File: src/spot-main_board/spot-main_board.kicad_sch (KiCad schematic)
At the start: 0 parts

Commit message: Start drawing schematics.
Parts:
- added A1: Arduino_UNO_R3, Module:Arduino_UNO_R3, symbol MCU_Module:Arduino_UNO_R3
- added D1: PTVS7V5Z1USK, Diode_SMD:Nexperia_DSN1608-2_1.6x0.8mm, symbol Diode:PTVS7V5Z1USK
- added EFB1, J1: Conn_01x02, symbol Connector_Generic:Conn_01x02
- added EFB2: Microwave Oven Transformer, symbol Transformer:TEZ0.5-D-1
- added EFB?: RED, symbol Device:LED
- added EFB?: BLUE, symbol Device:LED
- added J3: AudioJack2, symbol Connector_Audio:AudioJack2
- added J?: Screw_Terminal_01x08, symbol Connector:Screw_Terminal_01x08
- added PS2: TMF05112, Converter_ACDC:Converter_ACDC_TRACO_TMF_051xx_THT, symbol Converter_ACDC:TMF05112
- added Q1: BT139-600, Package_TO_SOT_THT:TO-220-3_Vertical, symbol Triac_Thyristor:BT139-600
- added Q2: Q_PMOS_DGS, symbol Transistor_FET:Q_PMOS_DGS
- added R? (x2): 470, symbol Device:R
- added RV1: R_Potentiometer, symbol Device:R_Potentiometer
- added U1: MOC3041M, symbol Relay_SolidState:MOC3041M
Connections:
- new net: J?.4 (Pin_4), R?.2
- new net: J?.5 (Pin_5), R?.2
- new net: A1.11 (A2), J?.7 (Pin_7)
- new net: A1.25 (D10), R?.1
- new net: A1.26 (D11), R?.1
- new net +12V: A1.8 (VIN), J?.6 (Pin_6), Q2.3 (S)
- new net +DC_OUT: D1.1 (K), PS2.4 (+Vout), Q2.1 (D)
- new net AC_L: J1.1 (Pin_1), PS2.1 (AC(L))
- new net AC_N: J1.2 (Pin_2), PS2.2 (AC(N)), Q1.2 (A2)
- new net CONN_+5V: RV1.1
- new net CONN_GND: EFB?.1 (K), EFB?.1 (K), RV1.3
- new net GND: A1.29 (GND), A1.6 (GND), A1.7 (GND), D1.2 (A), J?.8 (Pin_8), PS2.3 (-Vout), Q2.2 (G)
- no-connect marks 0 -> 12
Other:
- note added: "230 VAC in"
- note added: "External interface"
- note added: "~10 mA"
- title: (none) -> Spot

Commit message: Add Electronics Block Diagram. Continue work on schematics.
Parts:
- removed EFB1: Conn_01x02, symbol Connector_Generic:Conn_01x02
- removed EFB2: Microwave Oven Transformer, symbol Transformer:TEZ0.5-D-1
- removed EFB?: RED, symbol Device:LED
- removed EFB?: BLUE, symbol Device:LED
- removed J3: AudioJack2, symbol Connector_Audio:AudioJack2
- removed RV1: R_Potentiometer, symbol Device:R_Potentiometer
- added J?: Conn_01x02, symbol Connector_Generic:Conn_01x02
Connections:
- net AC_L: now also J?.1 (Pin_1)
- net at J?.2 (Pin_2): now also A1.23 (D8)
- net at J?.3 (Pin_3): now also A1.24 (D9)
- net at Q1.1 (A1): now also J?.2 (Pin_2)
- net +5V: now reaches A1.5 (+5V)
- no-connect marks 12 -> 11
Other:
- note added: "To MOT primary coil"
- note removed: "External interface"
- company: (none) -> Anker Bjerkestrand
- moved on the sheet: A1, D1, J1, J?, PS2, Q1, Q2, R?, U1

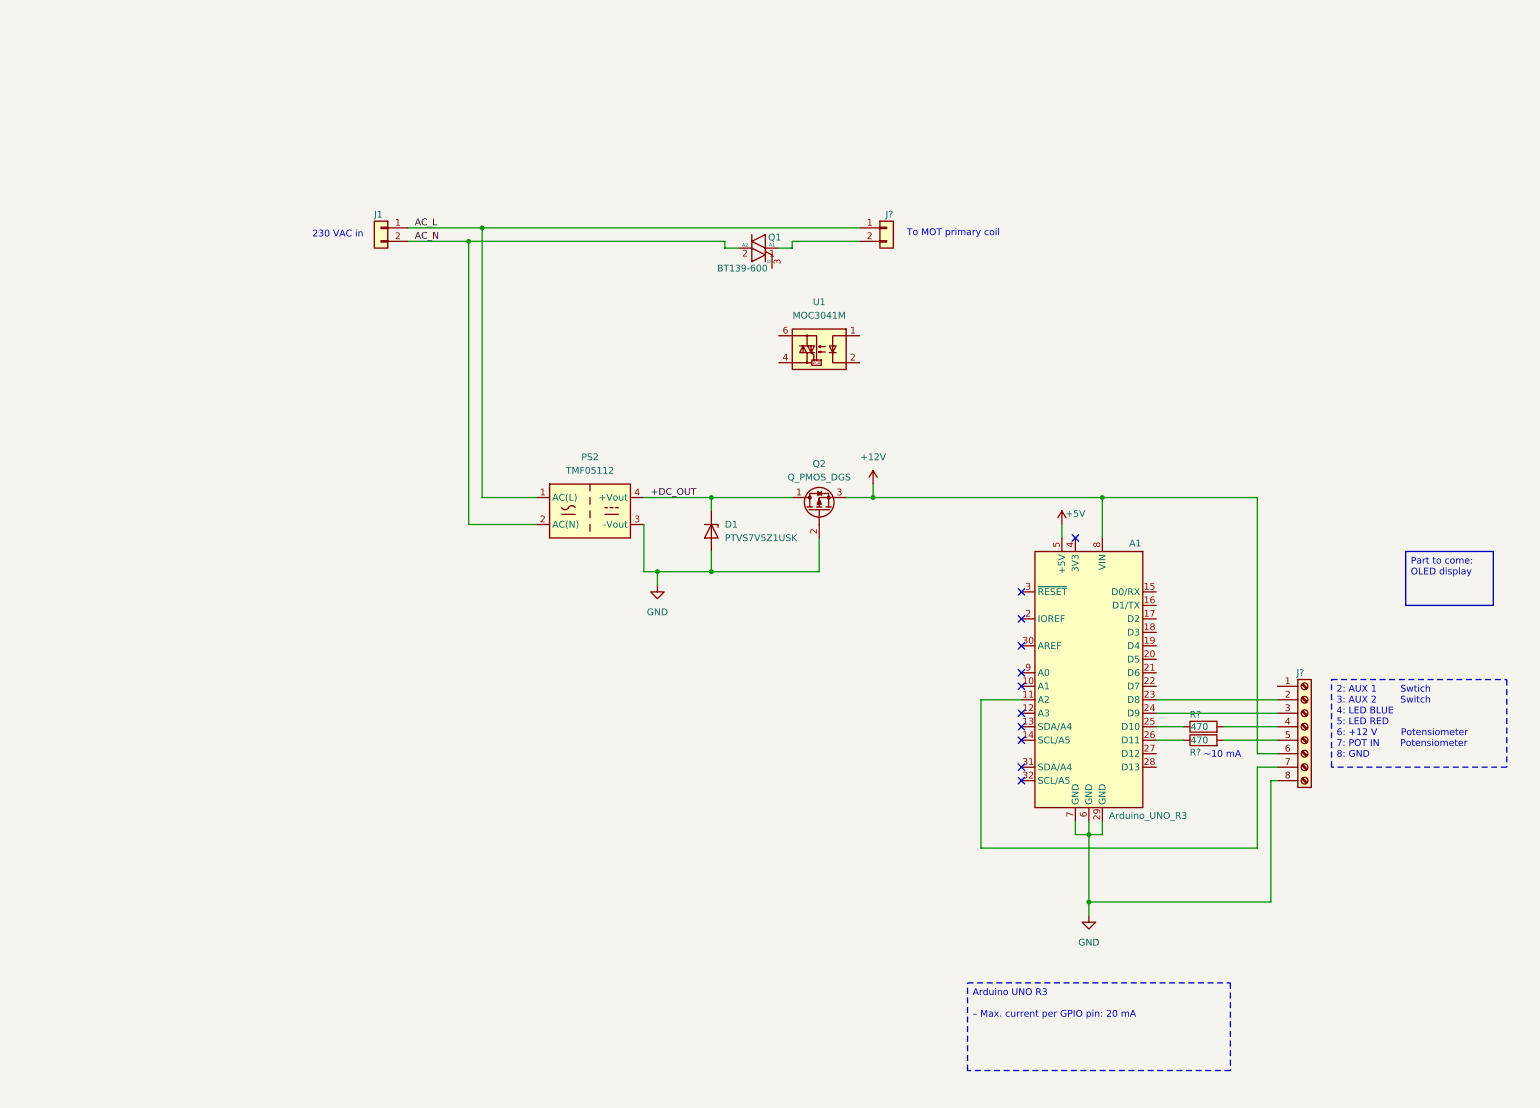
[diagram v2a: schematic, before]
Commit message: Add kidibom.py file. Add example circuitry for triac and driver.
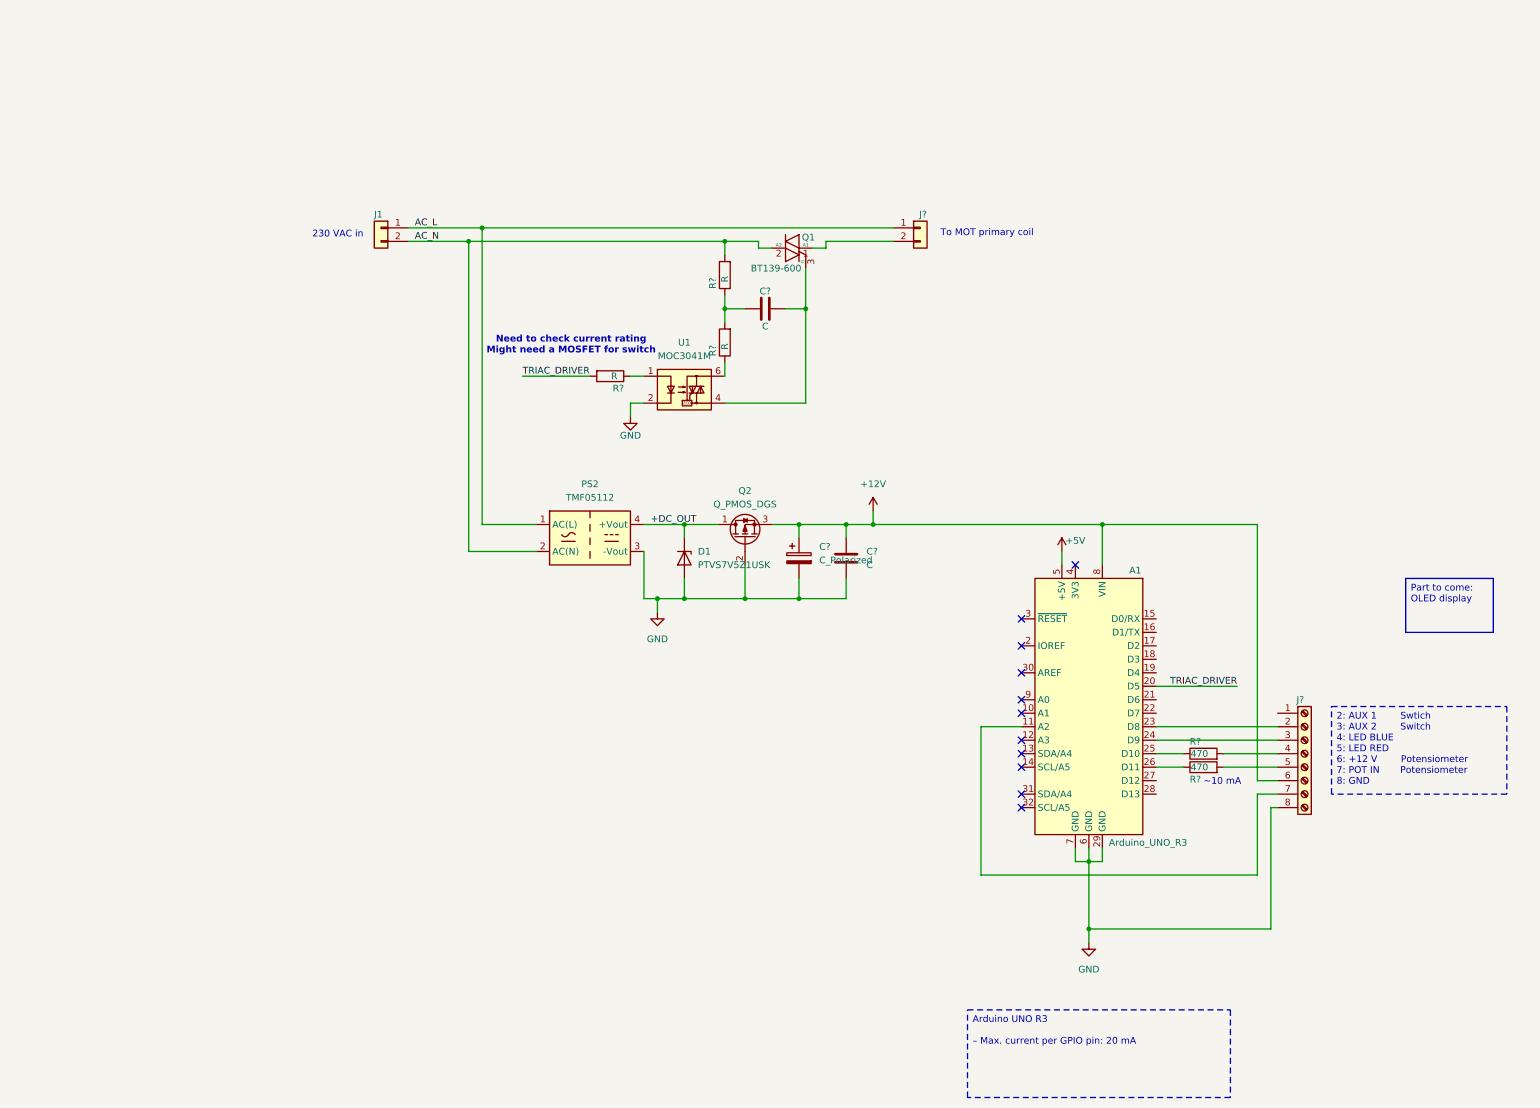
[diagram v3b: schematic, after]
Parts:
- added C?: C_Polarized, symbol Device:C_Polarized
- added C? (x2): C, symbol Device:C
- added R? (x3): R, symbol Device:R
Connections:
- net +12V: now also C?.1, C?.1
- net AC_N: now also R?.2
- net GND: now also U1.2, C?.2, C?.2
- net at Q1.3 (G): now also U1.4, C?.2
- net TRIAC_DRIVER: now reaches A1.20 (D5)
- net TRIAC_DRIVER: now also R?.2
- net at U1.1: now also R?.1
- net at U1.6: now also R?.1
- new net: C?.1, R?.1, R?.2
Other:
- note added: "Need to check current rating Might need a MOSFET for switch"
- moved on the sheet: A1, D1, J?, PS2, Q1, Q2, R?, U1

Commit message: Finish schematics. Start adding footprints and choosing components.
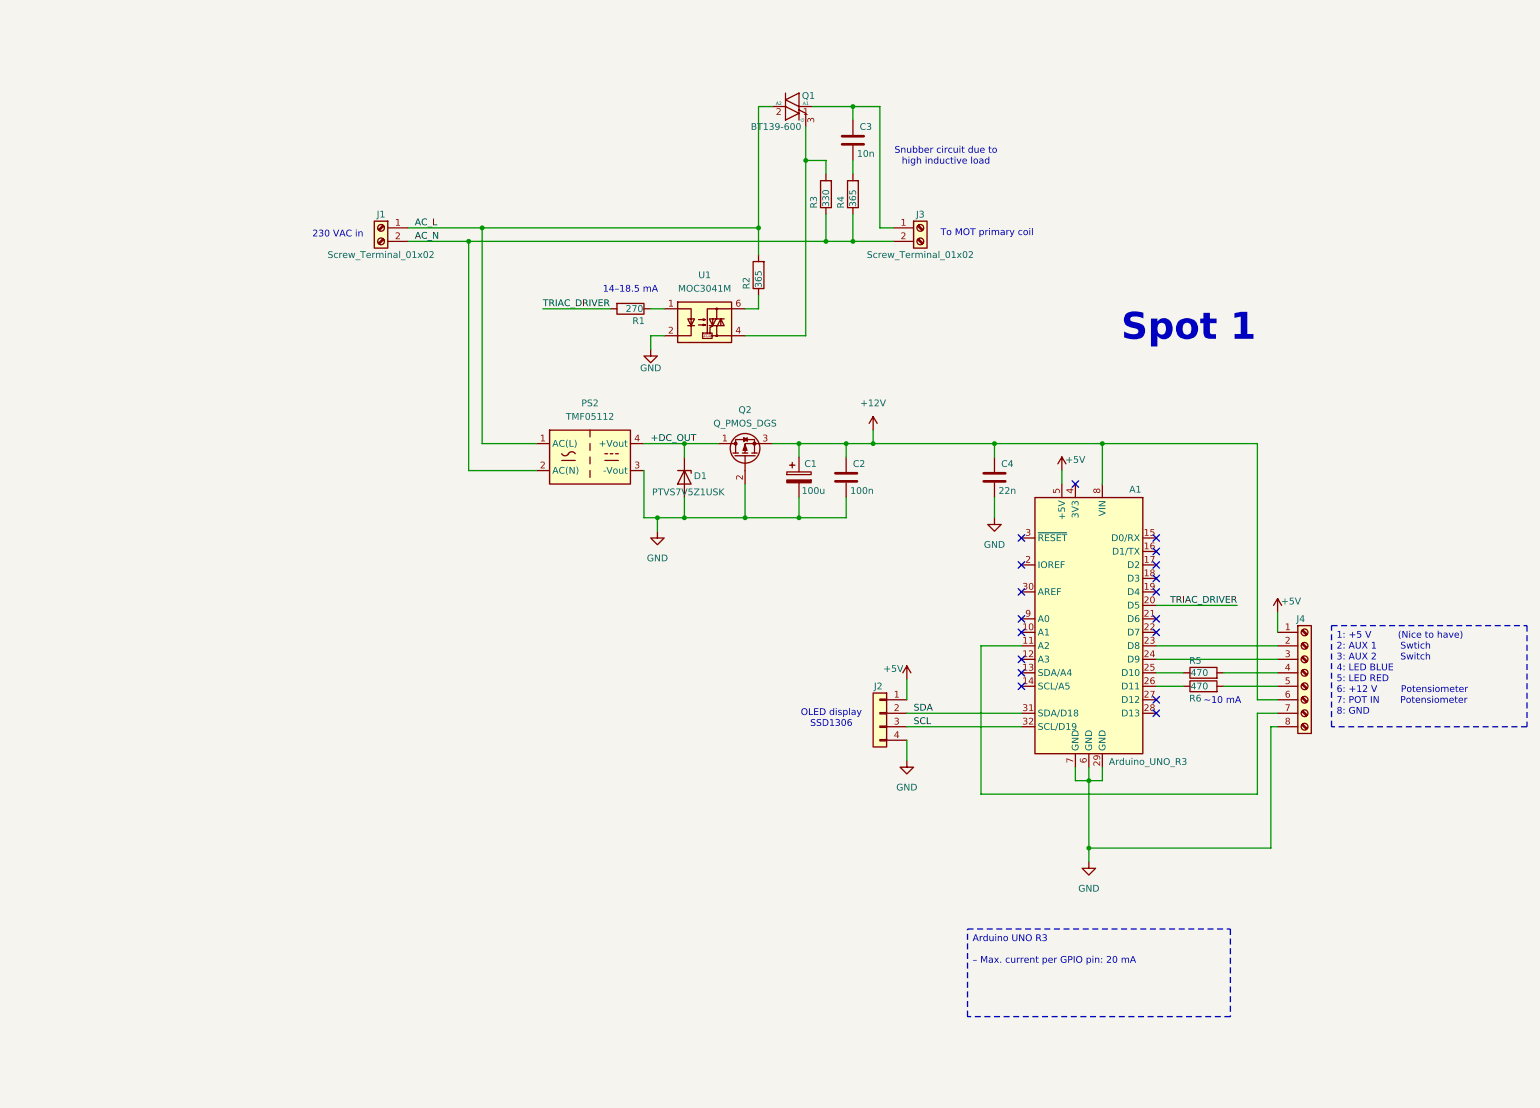
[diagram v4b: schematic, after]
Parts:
- removed C?: C, symbol Device:C
- removed R?: R, symbol Device:R
- added C3: 10n, Capacitor_THT:C_Rect_L13.5mm_W5.0mm_P10.00mm_FKS3_FKP3_MKS4, symbol Device:C
- added C4: 22n, Capacitor_SMD:C_1206_3216Metric, symbol Device:C
- added J2: Conn_01x04, Connector_PinHeader_2.54mm:PinHeader_1x04_P2.54mm_Vertical, symbol Connector_Generic:Conn_01x04
- added R3: 330, symbol Device:R
- added R4: 365, symbol Device:R
- A1: footprint Module:Arduino_UNO_R3 -> Module:Arduino_UNO_R3_WithMountingHoles
- C1: renamed from C?; value C_Polarized -> 100u
- C2: renamed from C?; value C -> 100n; footprint (none) -> Capacitor_SMD:C_1206_3216Metric; DigiKey PN (none) -> 1763-1206B104J101N-ND; MPN (none) -> 1206B104J101N; Manufacturer (none) -> Knowles Novacap
- J1: value Conn_01x02 -> Screw_Terminal_01x02; footprint (none) -> Connector_Phoenix_MC_HighVoltage:PhoenixContact_MCV_1,5_2-G-5.08_1x02_P5.08mm_Vertical; symbol Connector_Generic:Conn_01x02 -> Connector:Screw_Terminal_01x02; DigiKey PN (none) -> 277-1247-ND; MPN (none) -> 1729128; Manufacturer (none) -> Phoenix Contact
- J3: renamed from J?; value Conn_01x02 -> Screw_Terminal_01x02; footprint (none) -> Connector_Phoenix_MC_HighVoltage:PhoenixContact_MCV_1,5_2-G-5.08_1x02_P5.08mm_Vertical; symbol Connector_Generic:Conn_01x02 -> Connector:Screw_Terminal_01x02; DigiKey PN (none) -> 277-1247-ND; MPN (none) -> 1729128; Manufacturer (none) -> Phoenix Contact
- J4: renamed from J?; footprint (none) -> Connector_Phoenix_MC_HighVoltage:PhoenixContact_MCV_1,5_8-G-5.08_1x08_P5.08mm_Vertical; DigiKey PN (none) -> 277-1253-ND; MPN (none) -> 1729186; Manufacturer (none) -> Phoenix Contact
- R1: renamed from R?; value R -> 270; footprint (none) -> Resistor_SMD:R_1206_3216Metric
- R2: renamed from R?; value R -> 365
- R5, R6: renamed from R?; footprint (none) -> Resistor_SMD:R_1206_3216Metric
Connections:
- net +12V: now also C4.1
- net +5V: now also J4.1 (Pin_1), J2.1 (Pin_1)
- net AC_L: now also Q1.2 (A2), R2.2; no longer J3.1 (Pin_1)
- net AC_N: now also J3.2 (Pin_2), R3.1, R4.1; no longer Q1.2 (A2)
- net GND: now also C4.2, J2.4 (Pin_4)
- net at Q1.1 (A1): now also J3.1 (Pin_1), C3.1; no longer J3.2 (Pin_2)
- net at Q1.3 (G), U1.4: now also R3.2
- net SDA: now reaches A1.31 (SDA/D18)
- net SDA: now also J2.2 (Pin_2)
- net SCL: now reaches A1.32 (SCL/D19)
- net SCL: now also J2.3 (Pin_3)
- new net: C3.2, R4.2
- no-connect marks 11 -> 18
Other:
- note added: "14–18.5 mA"
- note added: "OLED display SSD1306"
- note added: "Snubber circuit due to high inductive load"
- note added: "Spot 1"
- note removed: "Need to check current rating Might need a MOSFET for switch"
- moved on the sheet: A1, C1, C2, D1, J4, PS2, Q1, Q2, R1, R2, R5, R6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
